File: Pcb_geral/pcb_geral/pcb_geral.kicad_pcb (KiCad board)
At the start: 2 copper layers, 21 parts, among them U1 LM2594M-3.3, U2 LM2596S-5, U3 STM32F103C6Tx, U4 TJA1051T, Y2 8Mhz

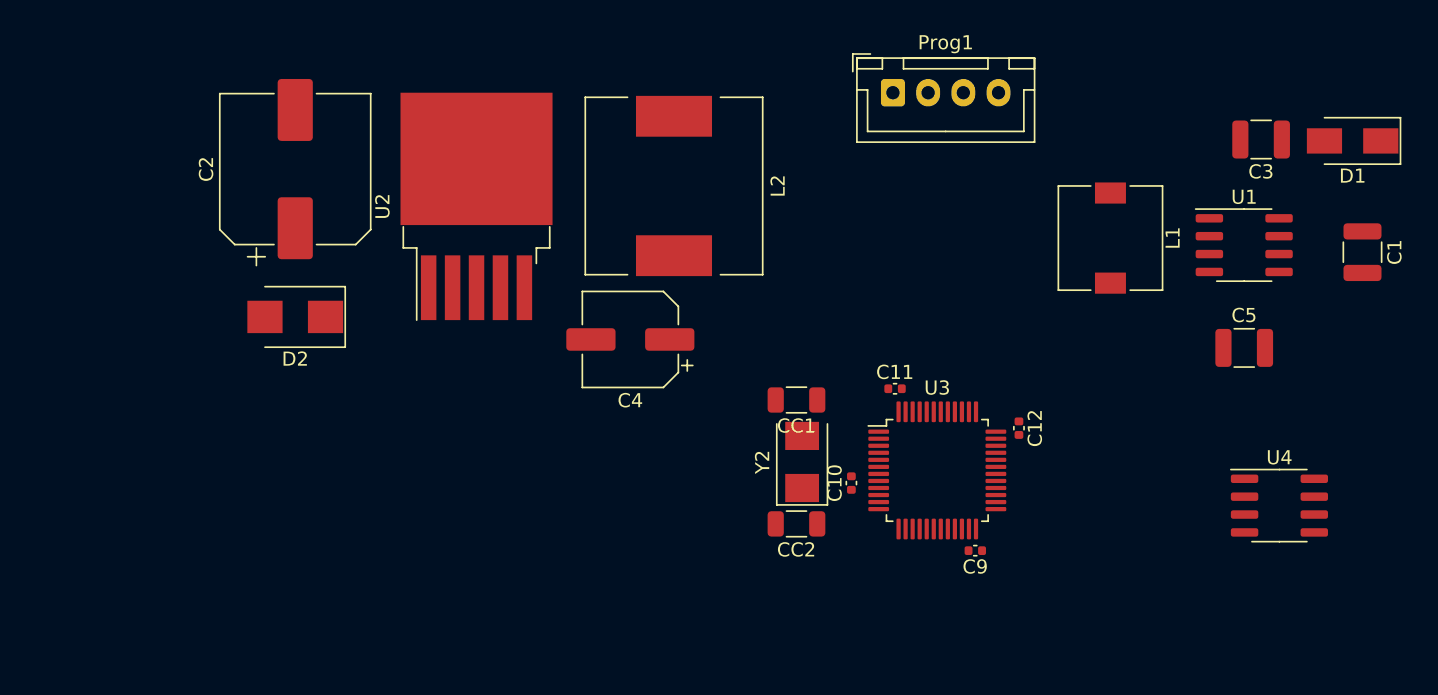
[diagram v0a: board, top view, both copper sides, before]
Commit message: cristal clock posicionado, seguindo as boas praticas de desenho de PCI
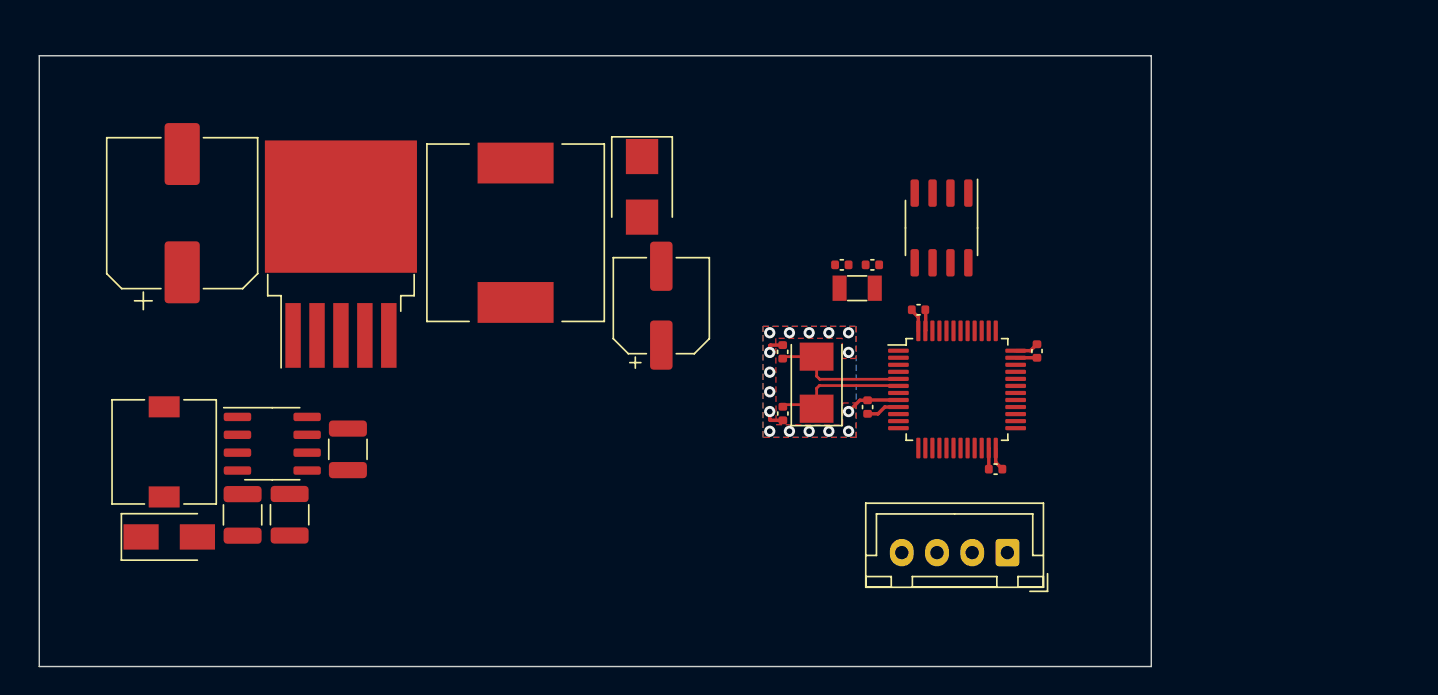
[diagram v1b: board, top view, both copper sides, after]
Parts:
- added C6: 22pF, Capacitor_SMD:C_0402_1005Metric, F.Cu at (130.5, 49.8)
- added C7: 22pF, Capacitor_SMD:C_0402_1005Metric, F.Cu at (128.3, 49.8)
- added Y1: Crystal, Crystal:Crystal_SMD_3215-2Pin_3.2x1.5mm, F.Cu at (129.4, 51.5)
- CC1, CC2: footprint Capacitor_SMD:C_1206_3216Metric -> Capacitor_SMD:C_0402_1005Metric
- moved D1 88.6 mm to (80.5, 69.1), turned to 0 degrees
- moved C3 74.0 mm to (89.1, 67.5), turned to -90 degrees
- moved C1 73.4 mm to (93.2, 62.9)
- moved C5 72.1 mm to (85.8, 67.6), turned to -90 degrees
- moved U1 70.5 mm to (87.9, 62.5)
- moved L1 68.9 mm to (80.2, 63.1)
- moved Prog1 33.7 mm to (140.1, 70.2), turned to 180 degrees
- moved U4 31.1 mm to (135.4, 47.2), turned to -90 degrees
- moved D1 26.3 mm to (114.1, 44.3), turned to -90 degrees
- moved L2 11.7 mm to (105.2, 47.5)
- moved U2 10.2 mm to (92.7, 49.0)
- moved C7 8.62 mm to (81.5, 46.1)
- moved CC2 7.90 mm to (124.1, 60.4), turned to -90 degrees
- moved C9 5.97 mm to (139.2, 64.3)
- moved U3 5.92 mm to (136.5, 58.6)
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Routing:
- net GND: track 0.00 -> 11.4 mm, vias 0 -> 16
- net /OSC+: track 0.00 -> 9.93 mm
- net /OSC-: track 0.00 -> 9.77 mm
- net +3V3: track 0.00 -> 7.47 mm
- added copper zone on B.Cu, net GND
- added copper zone on F.Cu, net GND
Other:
- board outline added: 79 x 43.4 mm

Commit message: plano de alimentação, saparar dos planos alimentação do plano digital
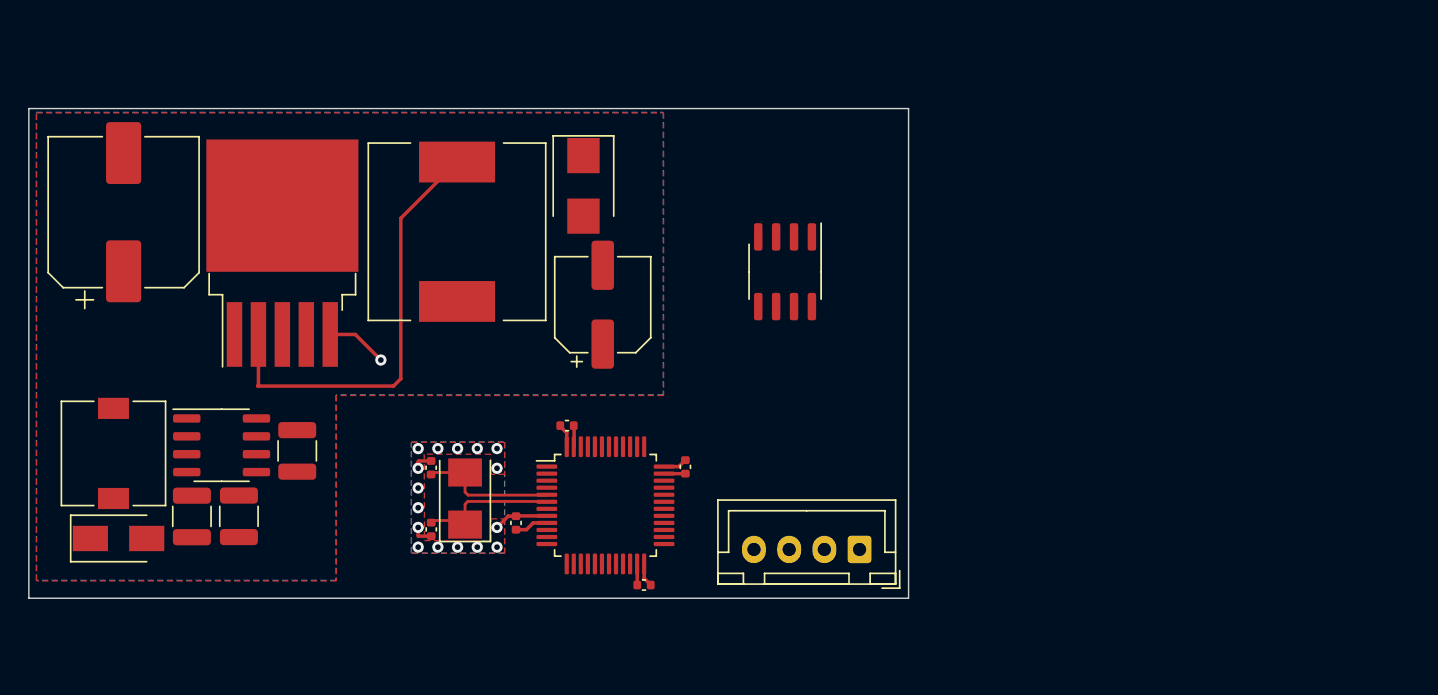
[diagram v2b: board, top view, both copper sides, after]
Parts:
- removed C6: 22pF, Capacitor_SMD:C_0402_1005Metric
- removed the C7 at (128.3, 49.8)
- removed Y1: Crystal, Crystal:Crystal_SMD_3215-2Pin_3.2x1.5mm
- moved C12 26.3 mm to (117.2, 64.2)
- moved C9 26.3 mm to (114.3, 72.5)
- moved C11 26.3 mm to (108.8, 61.2)
- moved CC2 26.3 mm to (99.2, 68.6)
- moved Y2 26.3 mm to (101.6, 66.4)
- moved C10 26.3 mm to (105.2, 68.1)
- moved CC1 26.3 mm to (99.2, 64.2)
- moved U3 26.3 mm to (111.5, 66.9)
- moved U4 11.5 mm to (124.3, 50.3)
- moved Prog1 10.5 mm to (129.6, 70.0)
- moved L2 4.16 mm to (101.0, 47.5)
- moved U2 4.16 mm to (88.6, 49.0)
- moved C7 4.16 mm to (77.3, 46.1)
- moved C8 4.16 mm to (111.3, 52.6)
- moved D1 4.16 mm to (110.0, 44.2)
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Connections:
- U3 pad 3: PC14 -> unconnected-(U3-Pad3)
- U3 pad 4: PC15 -> unconnected-(U3-Pad4)
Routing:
- net /Out_pwr_indutor: track 0.00 -> 31.1 mm
- net GND: track 11.4 -> 15.7 mm, vias 16 -> 17
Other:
- board size 79 x 43.4 mm -> 62.5 x 34.8 mm
- board text added: "Capibaja V 3.00 Voa Braia"
